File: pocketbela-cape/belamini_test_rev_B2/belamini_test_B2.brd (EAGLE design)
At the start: 55 x 35 mm, 10 parts, among them J1 M10SILK_FEMALE_PTH, J3 22-23-2031, J4 22-23-2031

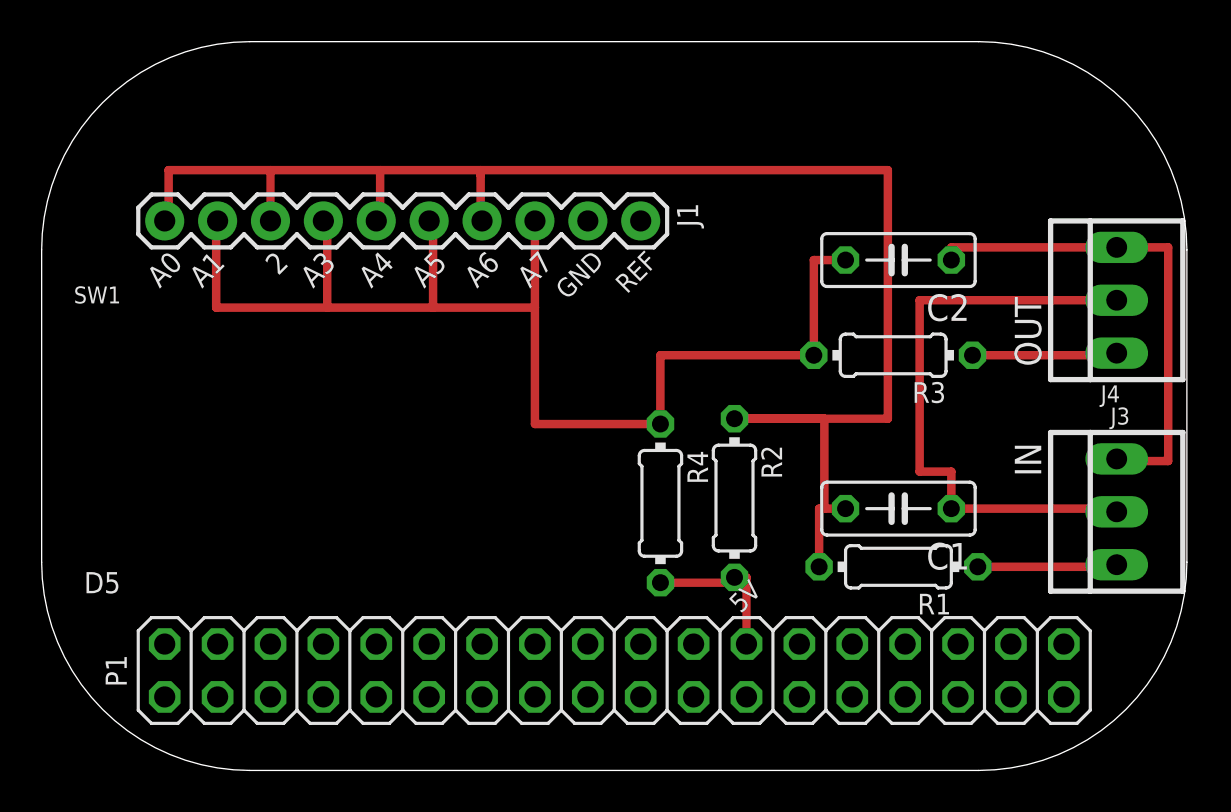
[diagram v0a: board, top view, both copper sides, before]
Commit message: belamini test jig attempt 2
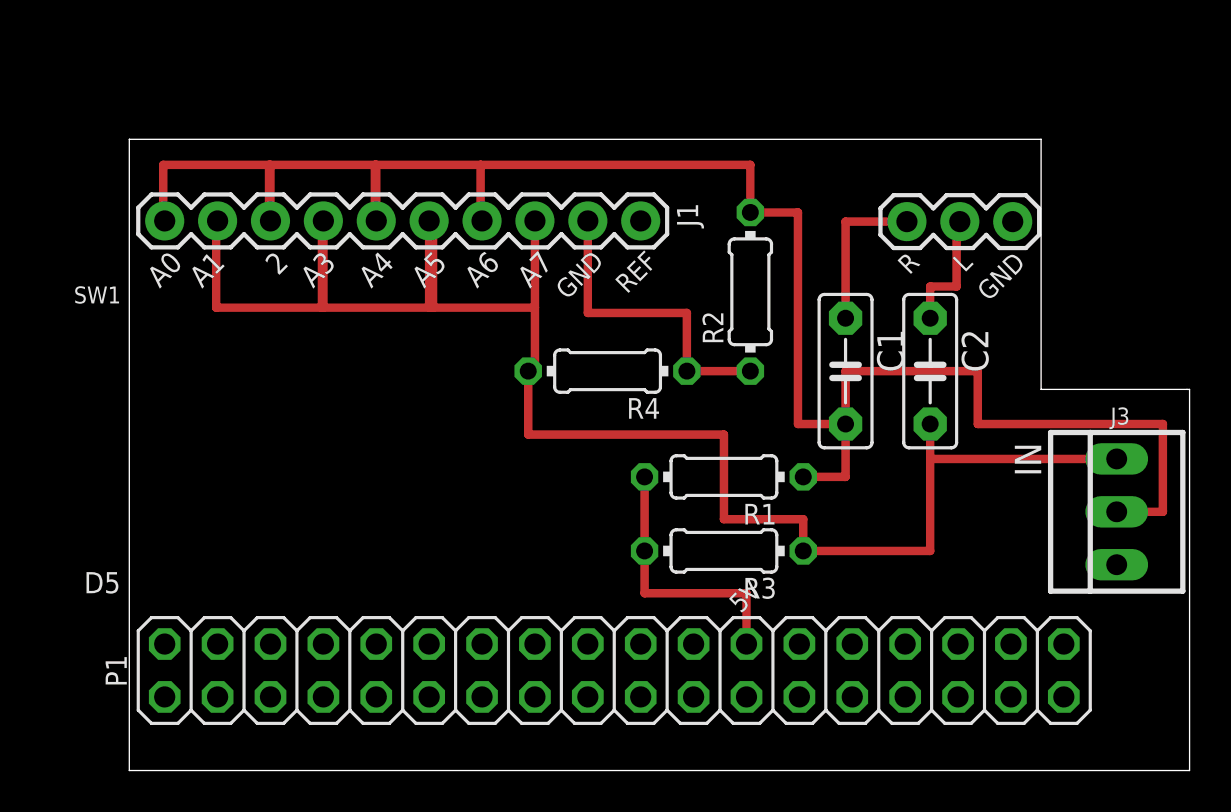
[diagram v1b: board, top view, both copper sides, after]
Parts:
- removed J4: 22-23-2031, con-molex:22-23-2031
- added J2: DNI, SparkFun-Connectors:1X03
- C1, C2: device resistor:C050-025X075 -> capacitor-wima:C5B2.5
- moved R3 12.4 mm to (31.2, 13.7)
- moved R2 9.94 mm to (32.5, 26.2), turned to 90 degrees
- moved R1 9.43 mm to (31.2, 17.3)
- moved C1 7.08 mm to (37.1, 22.4), turned to 270 degrees
- moved R4 6.84 mm to (25.7, 22.4), turned to 180 degrees
- moved C2 5.55 mm to (41.1, 22.4), turned to 270 degrees
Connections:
- removed net N$1: C2.2, J1.3, J1.5, J1.7, J1.9, R3.2, R4.1
- removed net N$2: C1.2, J1.10, J1.4, J1.6, J1.8, R1.2, R2.1
- removed net N$3: C1.1, J3.2, J4.2
- removed net N$4: C2.1, J3.3, J4.3
- new net AGND: J1.2, R2.1, R4.1
- new net LEFT: C1.2, J1.10, J1.4, J1.6, J1.8, J3.2, R1.1, R2.2
- new net LEFT_LOP: C2.1, J2.2
- new net RIGHT: C2.2, J1.3, J1.5, J1.7, J1.9, J3.3, R3.1, R4.2
- new net RIGHT_LOP: C1.1, J2.3
- net +5V_SYS: now also R1.2, R3.2; no longer R2.2, R4.2
- net GND: now also J2.1; no longer J3.1, J4.1, R1.1, R3.1
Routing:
- net LEFT: track 0.00 -> 93.0 mm
- net RIGHT: track 0.00 -> 86.8 mm
- net N$2: track 76.7 -> 0.00 mm
- net N$1: track 60.8 -> 0.00 mm
- net N$3: track 29.1 -> 0.00 mm
- net N$4: track 23.9 -> 0.00 mm
- net AGND: track 0.00 -> 15.0 mm
- net GND: track 13.8 -> 0.00 mm
- net RIGHT_LOP: track 0.00 -> 7.59 mm
- net LEFT_LOP: track 0.00 -> 6.06 mm
- net +5V_SYS: track 7.59 -> 12.9 mm
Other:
- board size 55 x 35 mm -> 50.9 x 30.3 mm
- board text added: "L"
- board text added: "R"
- board text removed: "OUT"
- board text removed: "P2"

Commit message: Line out is DC-coupled, so no need for external components
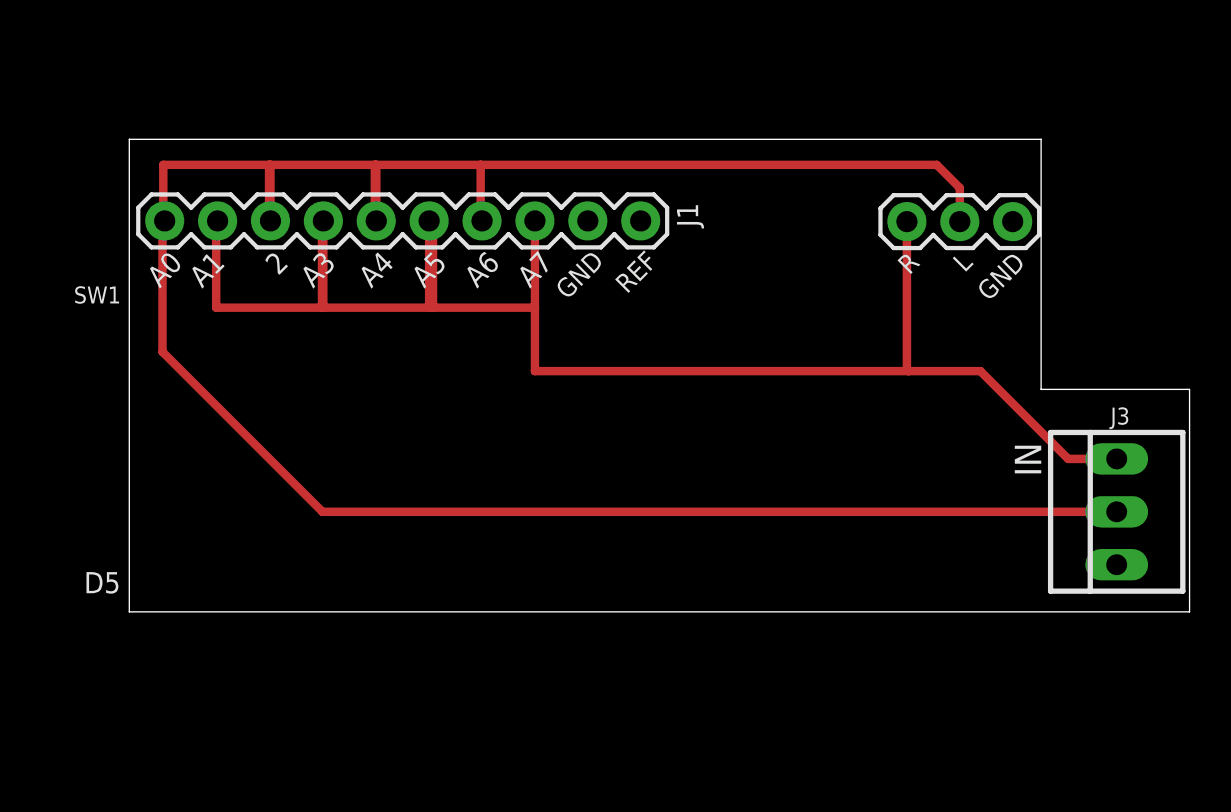
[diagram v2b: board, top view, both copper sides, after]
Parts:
- removed C1, C2: (no value), capacitor-wima:C5B2.5
- removed P1: (no value), pinhead:2X18
- removed R1, R2, R3, R4: (no value), resistor:0204/7
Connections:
- removed net +5V_SYS: P1.24, R1.2, R3.2
- removed net LEFT_LOP: C2.1, J2.2
- removed net RIGHT_LOP: C1.1, J2.3
- net AGND: no longer R2.1, R4.1
- net LEFT: now also J2.2; no longer C1.2, R1.1, R2.2
- net RIGHT: now also J2.3; no longer C2.2, R3.1, R4.2
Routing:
- net LEFT: track 93.0 -> 112.1 mm
- net AGND: track 15.0 -> 0.00 mm
- net +5V_SYS: track 12.9 -> 0.00 mm
- net RIGHT_LOP: track 7.59 -> 0.00 mm
- net RIGHT: track 86.8 -> 80.4 mm
- net LEFT_LOP: track 6.06 -> 0.00 mm
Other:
- board size 50.9 x 30.3 mm -> 50.9 x 22.7 mm
- board text removed: "5V"
